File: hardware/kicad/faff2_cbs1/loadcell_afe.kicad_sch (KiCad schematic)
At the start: 59 parts, among them J501 1729076, U501 ADS1235

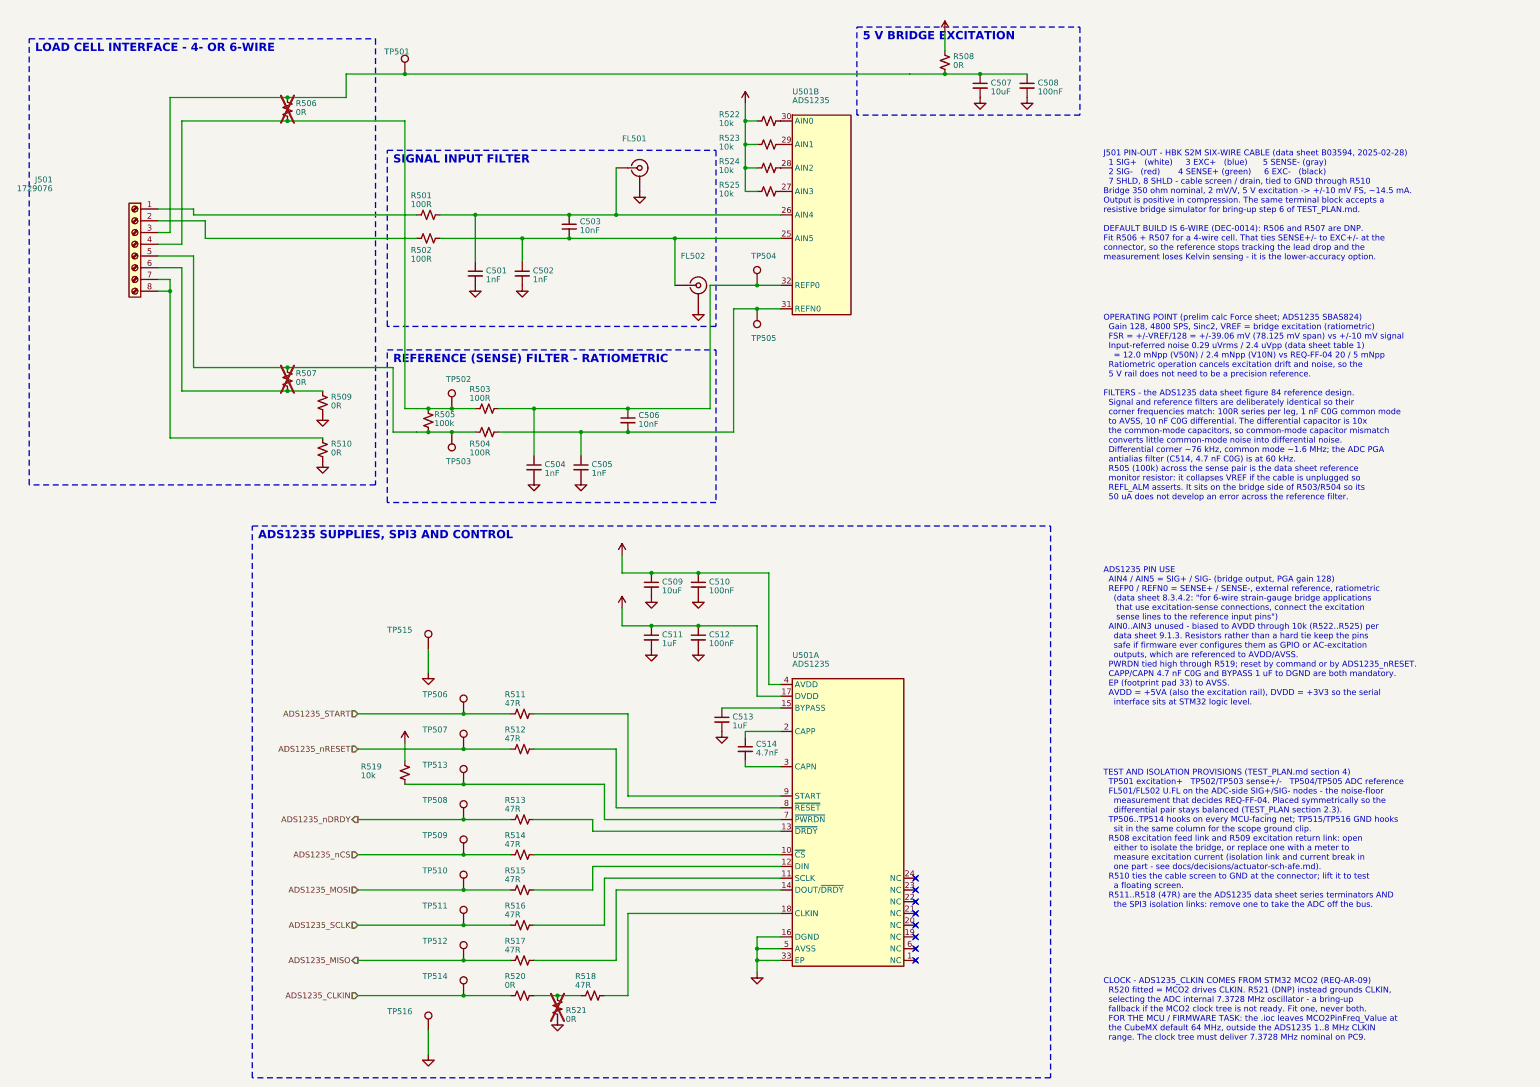
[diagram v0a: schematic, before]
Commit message: review r1: logic-analyser headers, U501 reference note, AFE/encoder fixes
Answers the captain's round-1 review points on loadcell_afe, linear_encoder,
temp_sense and nvm_calibration.

U501 and the reference (R1). The ADS1235 has no internal reference and no
reference output pin - REFP0/REFN0 are inputs. The reference is the load cell's
own excitation, sensed at the bridge, which is what makes the measurement
ratiometric. Documented in a 15-line note beside U501B's reference pins.

Logic-analyser headers (R2, R5). The Amodo keyed 10-way 0.1in socket
(8510-4500PL) replaces the per-net hooks:

  J502  loadcell_afe   CH0..CH7 = the whole SPI3 interface plus nDRDY, START,
                       nRESET and CLKIN; TP506..TP512 and TP514 removed
  J603  linear_encoder CH0..CH4 = the three receiver outputs plus ENC_SDO and
                       ENC_nPROG; TP602..TP607 removed

Both tap the driver side of the series terminators, so the header still sees the
bus when an isolation link is lifted. J602 is KEPT: it carries REQ-PS-09, its
pin 9 is +5V_ENC where the socket wants GND, and six of its signals are the
terminated RS-422 pairs that DEC-0018 ruling 1 keeps stub-free. Raised as a
decision; ruled option (a) and captain-ratified.

J601 (R3, R4). Reference text moved off the body; the project-local
FH12-10S-0.5SH(55) symbol now shows pin numbers and names every pin (1..10,
MP1/MP2), matching the FH35C house exemplar. Fixed in faff2_periph.kicad_sym
and in the sheet's embedded copy, so no lib_symbol_mismatch.

5 V read-head supply (R6). R608, R609 and D602 are DNP parallel positions on
R601, FB601 and D601. Not for current sharing - the ferrite alone has 4x margin
on the CALC budget - but for bring-up: a shunt at R608 meters head current in
circuit, R609 bypasses the bead, D602 is a second SC-79 clamp. Moving D601 up
to make room also cleared its value text off the ENC_nPROG label and its ground
triangle off the ENC_nPROG wire.

temp_sense C701/C702 (R7). Both had their groun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
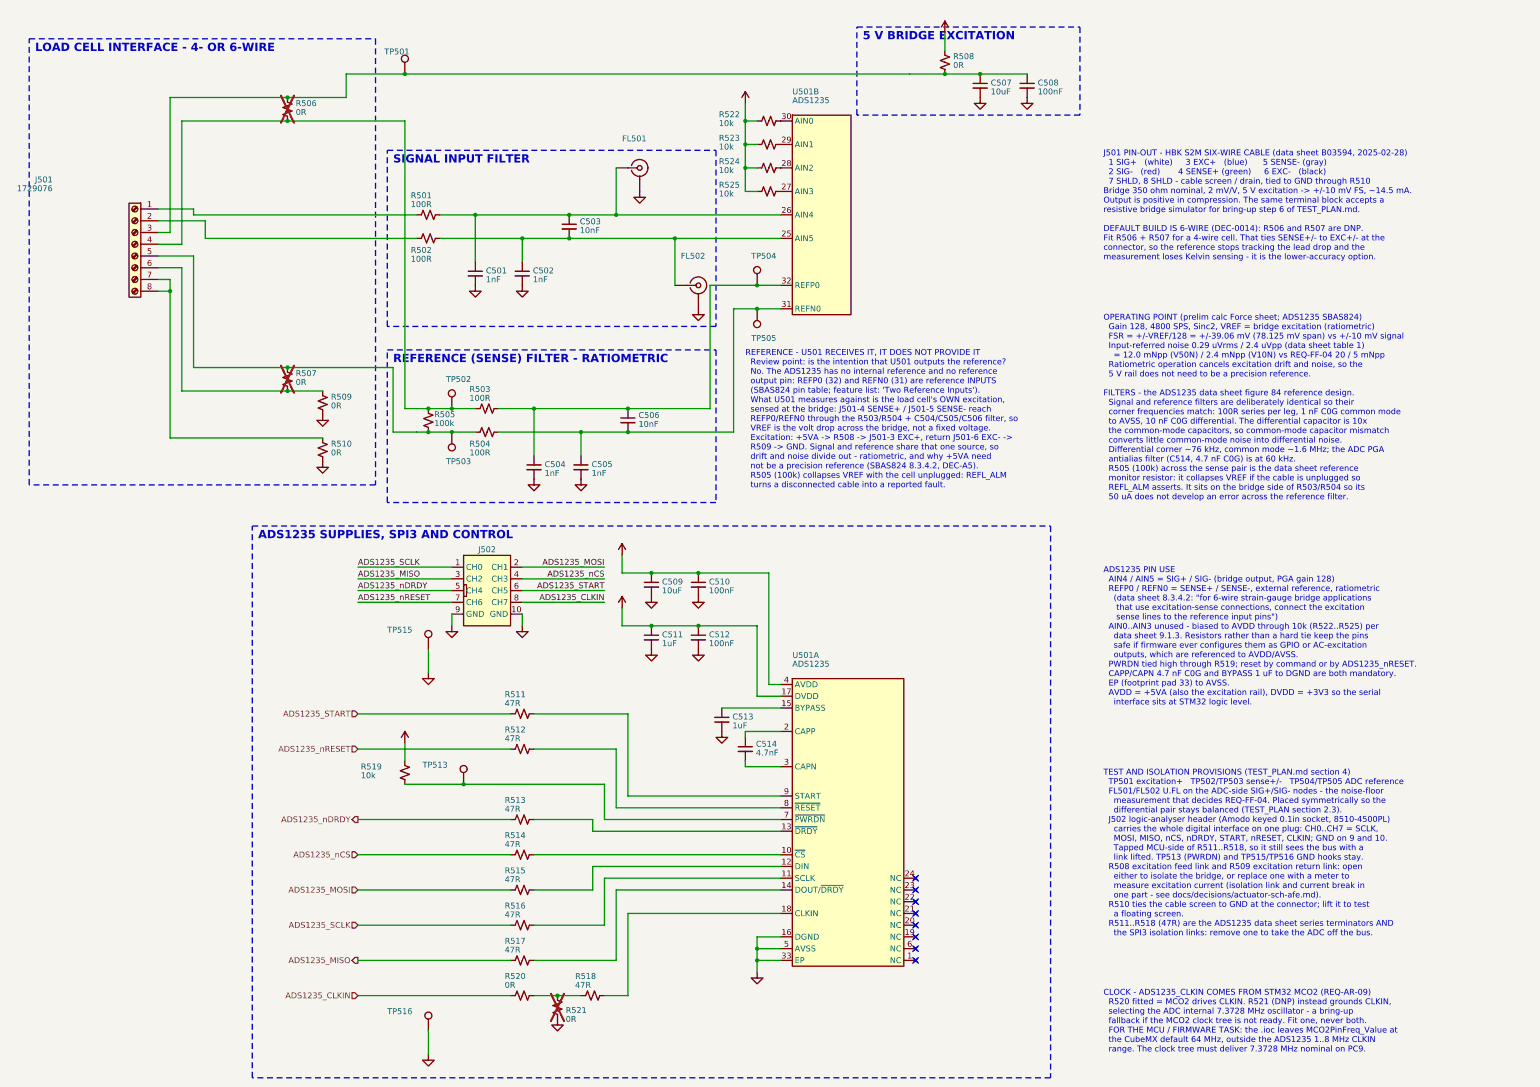
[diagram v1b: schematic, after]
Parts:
- removed TP506, TP507, TP508, TP509, TP510, TP511, TP512, TP514: TestPoint, Amodo:KeystoneMiniatureTestLoop, symbol Amodo_Connectors:TestPointHook
- added J502: 8510-4500PL, Amodo:8510-4500PL_LOGIC_TEST, symbol Amodo_Connectors:Header_Female_10-way_2-row_Straight_2.54mm_THT__KEYED_LOGIC_TE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
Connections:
- net ADS1235_CLKIN: now also J502.8 (CH7)
- net ADS1235_MISO: now also J502.3 (CH2)
- net ADS1235_MOSI: now also J502.2 (CH1)
- net ADS1235_SCLK: now also J502.1 (CH0)
- net ADS1235_START: now also J502.6 (CH5)
- net ADS1235_nCS: now also J502.4 (CH3)
- net ADS1235_nDRDY: now also J502.5 (CH4)
- net ADS1235_nRESET: now also J502.7 (CH6)
- net GND: now also J502.10 (GND), J502.9 (GND)
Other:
- note added: "REFERENCE - U501 RECEIVES IT, IT DOES NOT PROVIDE IT Review point: is the intention that U501 outputs the reference? No. The ADS1235 has no internal reference and no reference output pin: REFP0 (32) and REFN0 (31) are reference INPUTS (SBAS824 pin table; feature list: 'Two Reference Inputs'). What U501 measures against is the load cell's OWN excitation, sensed at the bridge: J501-4 SENSE+ / J501-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"
- note added: "TEST AND ISOLATION PROVISIONS (TEST_PLAN.md section 4) TP501 excitation+ TP502/TP503 sense+/- TP504/TP505 ADC reference FL501/FL502 U.FL on the ADC-side SIG+/SIG- nodes - the noise-floor measurement that decides REQ-FF-04. Placed symmetrically so the differential pair stays balanced (TEST_PLAN section 2.3). J502 logic-analyser header (Amodo keyed 0.1in socket, 8510-4500PL) carries the whole digit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"
- note removed: "TEST AND ISOLATION PROVISIONS (TEST_PLAN.md section 4) TP501 excitation+ TP502/TP503 sense+/- TP504/TP505 ADC reference FL501/FL502 U.FL on the ADC-side SIG+/SIG- nodes - the noise-floor measurement that decides REQ-FF-04. Placed symmetrically so the differential pair stays balanced (TEST_PLAN section 2.3). TP506..TP514 hooks on every MCU-facing net; TP515/TP516 GND hooks sit in the same column f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"

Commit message: review r1 final sweep: power labels, TP silkscreen names, text overlaps
The captain's design-wide pass, run once the per-sheet batches had landed.
Presentation only: ERC 0 errors / 0 warnings at severity-all, 404 components,
251 nets, and every per-net node set identical to the pre-sweep export.

  power labels   92 rail names were hidden on loadcell_afe, motor_drive and
                 temp_sense - all 285 power symbols now read, placed to the
                 house pattern (GND below the symbol, rail arrows above)
  test points    66 of 83 still carried the library default "TestPoint". All
                 83 now name what they measure, from the net they actually
                 land on in the netlist; longest is 5 characters
  text overlap   16 collisions cleared design-wide, four of them sub-millimetre
                 ones the bundled checker passes because it under-measures text
  GND upside down  none - 0 of 285 power symbols is rotated or mirrored
  graphic/wire   one: power_rails block D's bottom border lay along the last
                 PWR_FLAG's wire; the flag column moved up 2.54

The overlap checker turns out to have three separable blind spots, each settled
here by measuring a render rather than by reading the format: it grows every
text field rightward regardless of justify/mirror/180-rotation, so its box is a
mirror image of the truth for those and it both invents and misses collisions;
it measures text at ~1.06 mm per character where the real advance is ~1.19; and
it reflects a rotated symbol's body about the origin. tools/sch_geom.py models
all three correctly and the design is clean under it design-wide. Two of that
model's own rules - notes growing up from their anchor, and labels taking no
180-degree justify flip - were bugs of mine that the checker caught first. The
render is what settles it; neither tool is authoritative alone.

Placement is searched rather than guessed: 177 newly visible fields are tried
against every wire, block border, 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
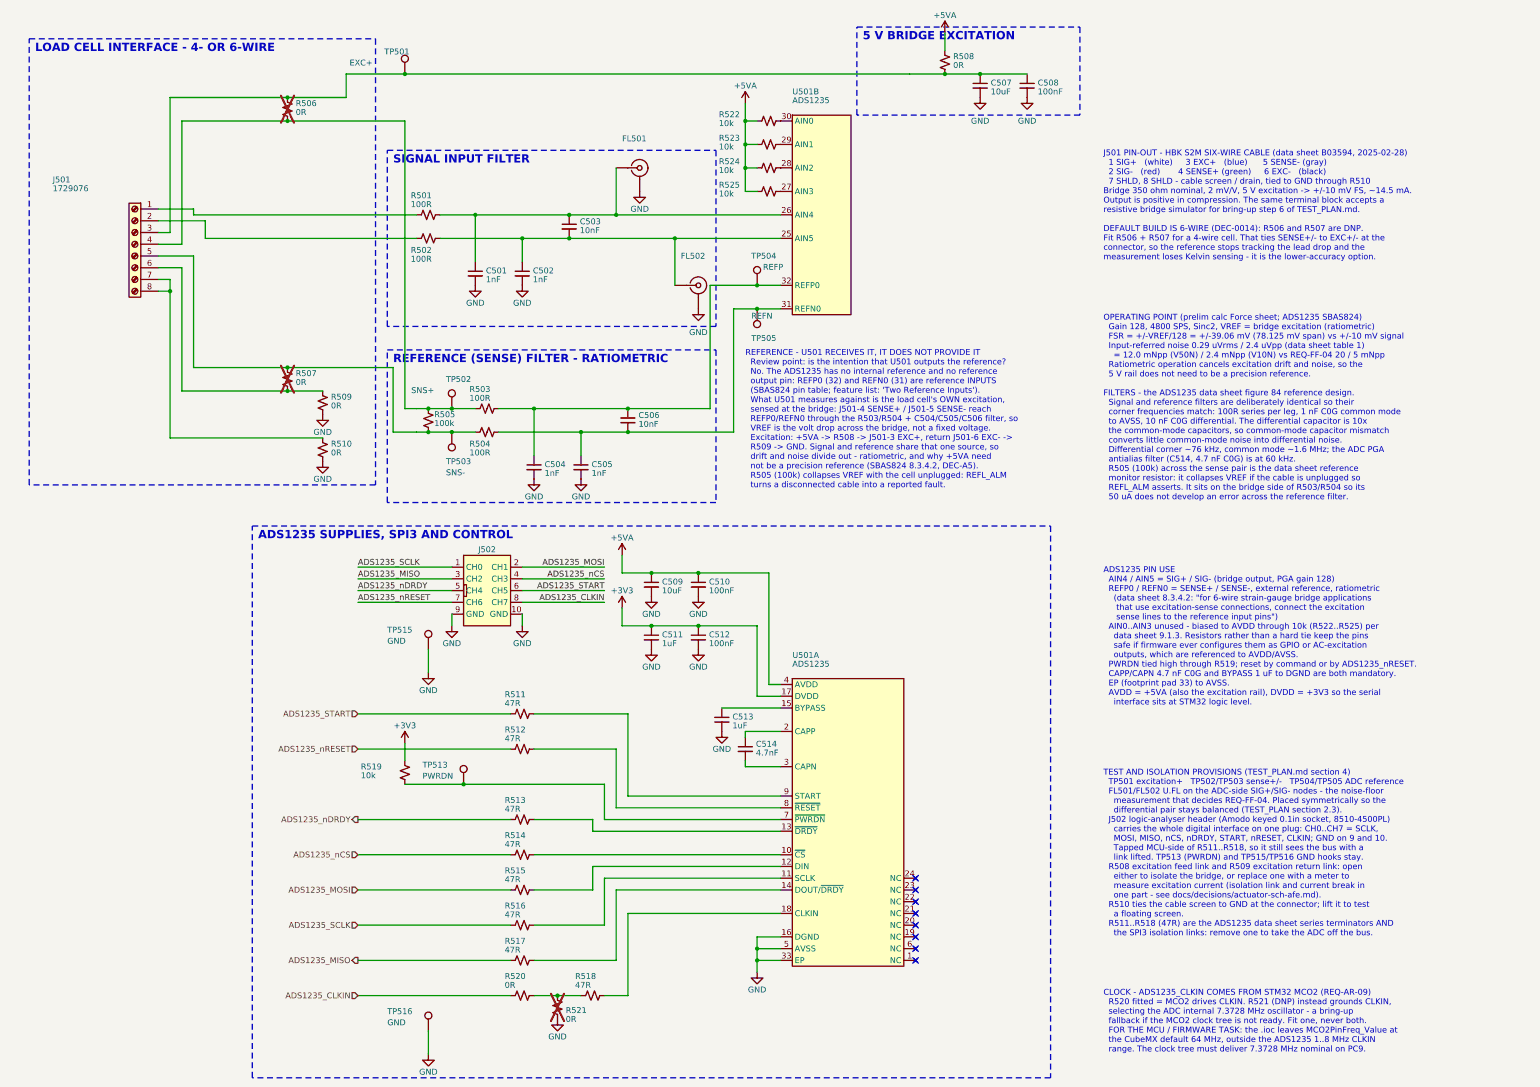
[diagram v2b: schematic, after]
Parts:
- TP501: value TestPoint -> EXC+
- TP502: value TestPoint -> SNS+
- TP503: value TestPoint -> SNS-
- TP504: value TestPoint -> REFP
- TP505: value TestPoint -> REFN
- TP513: value TestPoint -> PWRDN
- TP515, TP516: value TestPoint -> GND
